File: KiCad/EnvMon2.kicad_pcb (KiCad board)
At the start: 2 copper layers, 57.5 x 37 mm, 35 parts, among them J1 USB-C, J2 DC, J3 TEMP, M1 OLED1.5-RGB, SW1 SW_Push, SW2 SW_Push, SW3 SW_Push, U1 LMR16006+FB, U2 SCD41, U3 FT231XQ, U4 ESP32-PICO-MINI-02, U5 QR

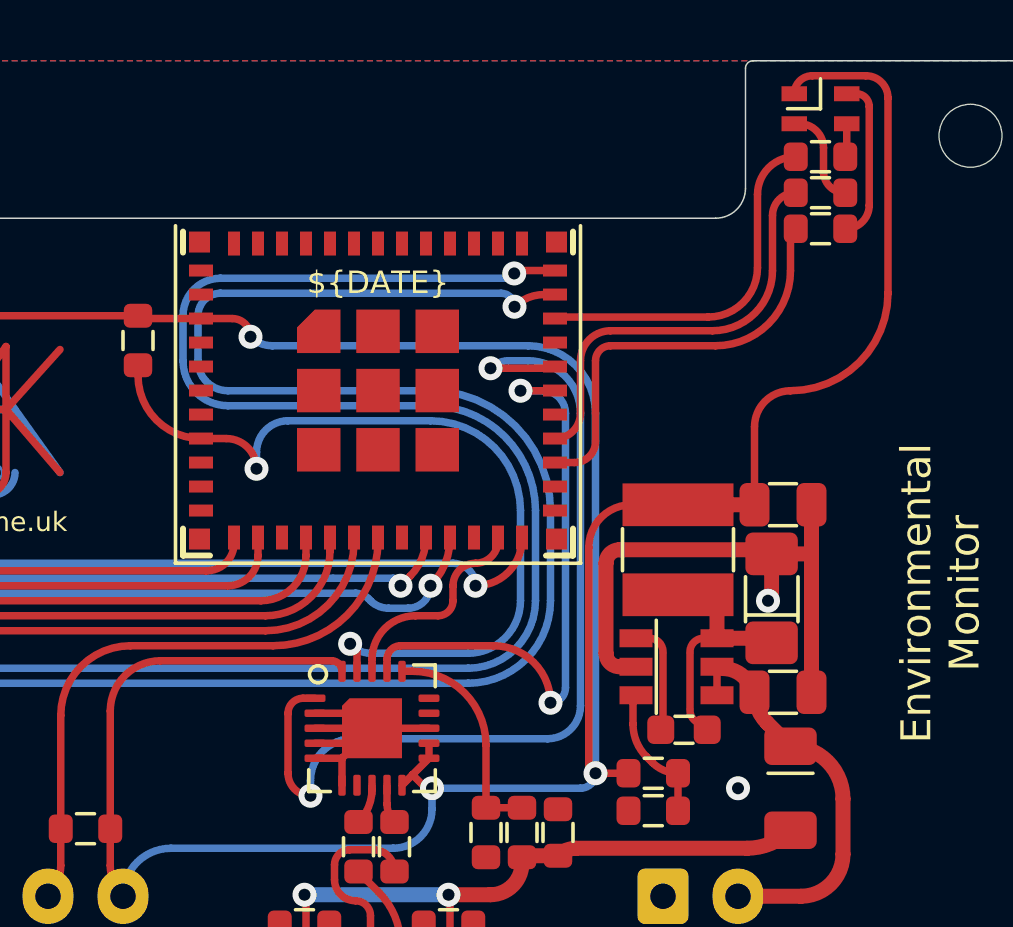
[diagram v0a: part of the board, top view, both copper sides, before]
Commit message: Updated regulator
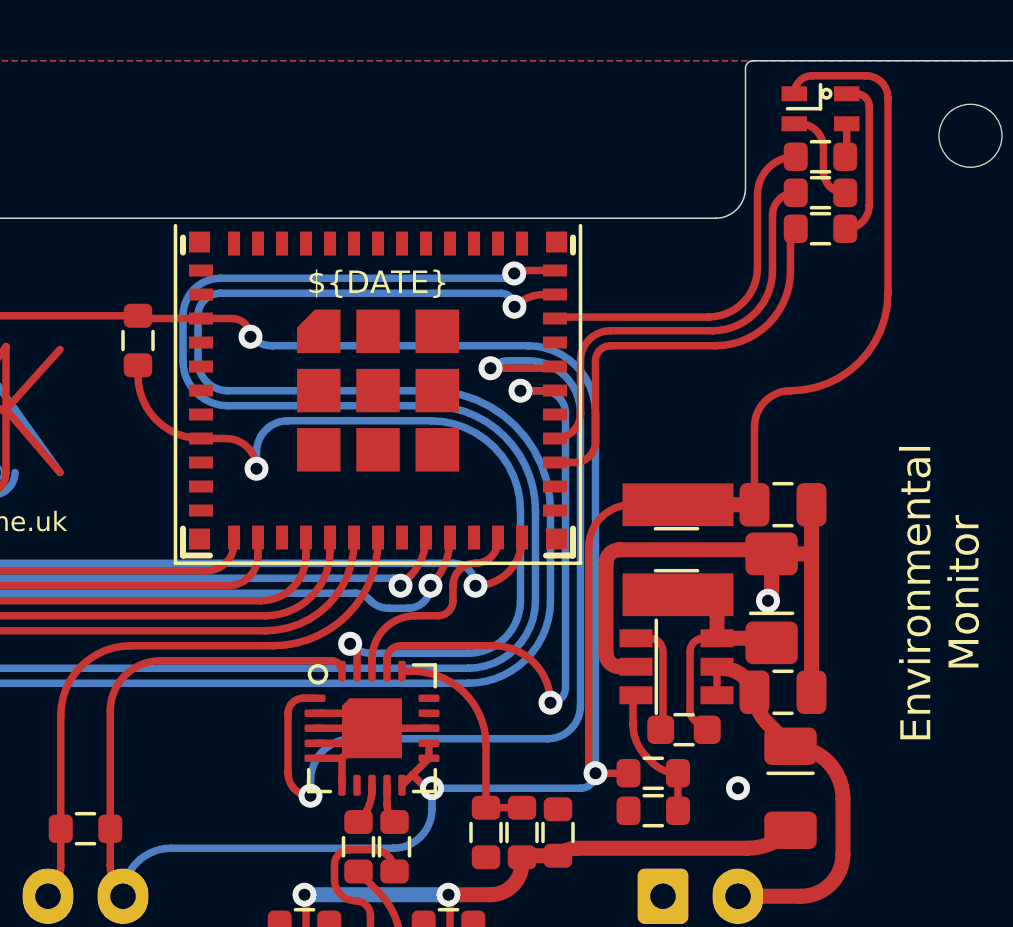
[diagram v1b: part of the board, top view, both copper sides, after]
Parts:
- C1: value 0.1uF -> 100nF; footprint RevK:Hidden -> RevK:C_0603_
- C2, C3: footprint RevK:Hidden -> RevK:C_0805_
- D1: footprint RevK:Hidden -> RevK:D_1206_
- L1: footprint RevK:Hidden -> RevK:L_4x4_

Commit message: Some PCB rework in progress
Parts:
- added J4: Shelly, RevK:Shelly, F.Cu at (141.7, 81.0)
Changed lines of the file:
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@@
     )
+  )
+  (footprint "RevK:Shelly" (layer "F.Cu")
+    (at 141.7 81 90)
+    (property "Sheetfile" "EnvMon2.kicad_sch")
+    (property "Sheetname" "")
+    (property "exclude_from_bom" "")
+    (attr through_hole exclude_from_bom)
+    (fp_text reference "J4" (at 0 -2.6 90 unlocked) (layer "F.SilkS") hide
+      (effects (font (size 1 1) (thickness 0.15)))
+    )
+    (fp_text value "Shelly" (at 0.2 3.7 90 unlocked) (layer "F.Fab") hide
+      (effects (font (size 1 1) (thickness 0.15)))
+    )
+    (fp_text user "⏚" (at 4.25 -0.8 135 unlocked) (layer "F.SilkS")
+      (effects (font (size 0.5 0.5) (thickness 0.08)))
+    )
+    (fp_text user "↑3" (at -3.37 -0.8 135 unlocked) (layer "F.SilkS")
+      (effects (font (size 0.5 0.5) (thickness 0.08)))
+    )
+    (fp_text user "0" (at 1.71 -0.8 135 unlocked) (layer "F.SilkS")
+      (effects (font (size 0.5 0.5) (thickness 0.08)))
+    )
+    (fp_text user "3V3" (at -0.83 -0.8 135 unlocked) (layer "F.SilkS")
+      (effects (font (size 0.5 0.5) (thickness 0.08)))
+    )
+    (fp_text user "↓1" (at -5.91 -0.8 135 unlocked) (layer "F.SilkS")
+      (effects (font (size 0.5 0.5) (thickness 0.08)))
+    )
+    (fp_text user "${REFERENCE}" (at 0 -2.6 90) (layer "F.Fab")
+      (effects (font (size 1 1) (thickness 0.15)))
+    )
+    (pad "1" thru_hole roundrect (at 5.08 0 90) (size 1.7 1.7) (drill 1) (layers *.Cu *.Mask) (roundrect_rratio 0)
+      (chamfer_ratio 0.3) (chamfer top_left)
+      (net 38 "O") (pinfunction "GND") (pintype "passive"))
+    (pad "2" thru_hole oval (at 2.54 0) (size 1.7 1.7) (drill 1) (layers *.Cu *.Mask)
+      (net 42 "I") (pinfunction "0") (pintype "passive"))
+    (pad "3" thru_hole oval (at 0 0) (size 1.7 1.7) (drill 1) (layers *.Cu *.Mask)
+      (net 12 "+3V3") (pinfunction "3V3") (pintype "passive"))
+    (pad "4" thru_hole oval (at -2.54 0) (size 1.7 1.7) (drill 1) (layers *.Cu *.Mask)
+      (net 47 "BOOT") (pinfunction "Rx") (pintype "passive"))
+    (pad "5" thru_hole oval (at -5.08 0) (size 1.7 1.7) (drill 1) (layers *.Cu *.Mask)
+      (net 11 "GND") (pinfunction "Tx") (pintype "passive"))
   )
   (footprint "RevK:C_0603_" (layer "F.Cu")

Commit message: Revised PCB for light sensor
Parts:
- added U6: VEML3235SL, RevK:VEML3235SL, F.Cu at (106.2, 63.8)
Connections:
- net CO2-SCL renamed SCL
- net CO2-SDA renamed SDA
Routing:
- net SDA: track 86.1 -> 114.7 mm, vias 2 -> 3
- net +3V3: track 151.9 -> 177.8 mm
- net BOOT: track 7.04 -> 31.7 mm, vias 0 -> 1
- net I: track 20.1 -> 37.1 mm, vias 2 -> 3
- net O: track 31.1 -> 47.9 mm, vias 2 -> 3
- net SCL: track 89.4 -> 104.5 mm, vias 2 -> 3
- net GND: track 12.1 -> 20.6 mm, vias 10 -> 12
- net R: track 14.0 -> 13.5 mm
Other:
- outline, holes or cut-outs redrawn

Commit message: Right angle
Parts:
- U6: value VEML3235SL -> VEML3235SL-RA; footprint RevK:VEML3235SL -> RevK:VEML3235SL-RA
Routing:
- net +3V3: track 177.8 -> 179.8 mm
- net SCL: track 104.5 -> 106.3 mm
- net SDA: track 114.7 -> 115.3 mm

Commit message: Library update
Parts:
- moved U6 1.40 mm to (107.6, 63.8)
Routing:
- net +3V3: track 179.8 -> 178.2 mm
- net SCL: track 106.3 -> 105.5 mm
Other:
- outline, holes or cut-outs redrawn

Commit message: Minor tweaks
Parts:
- J1: footprint RevK:USC16-TR-Round -> RevK:USC16-TR
- moved Logo1 0.95 mm to (109.6, 74.6)
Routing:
- net VBUS: track 22.2 -> 26.7 mm

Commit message: Library update
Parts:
- turned J4 to -90 degrees
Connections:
- J4 pad 1: O -> GND
- J4 pad 2: I -> BOOT
- J4 pad 4: BOOT -> I
- J4 pad 5: GND -> O
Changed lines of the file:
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@@
     )
   )
-  (property "DATE" "2022-11-28")
+  (property "DATE" "2022-12-14")
   (net 0 "")
   (net 1 "VBUS")
@@
   )
   (footprint "RevK:Shelly" (layer "F.Cu")
-    (at 141.7 81 90)
+    (at 141.7 81 -90)
     (property "Sheetfile" "EnvMon2.kicad_sch")
     (property "Sheetname" "")
     (property "exclude_from_bom" "")
     (attr through_hole exclude_from_bom)
-    (fp_text reference "J4" (at 0 -2.6 90 unlocked) (layer "F.SilkS") hide
-      (effects (font (size 1 1) (thickness 0.15)))
-    )
-    (fp_text value "Shelly" (at 0.2 3.7 90 unlocked) (layer "F.Fab") hide
-      (effects (font (size 1 1) (thickness 0.15)))
-    )
-    (fp_text user "3V3" (at -0.83 -0.8 135 unlocked) (layer "F.SilkS")
-      (effects (font (size 0.5 0.5) (thickness 0.08)))
-    )
-    (fp_text user "⏚" (at 4.25 -0.8 135 unlocked) (layer "F.SilkS")
-      (effects (font (size 0.5 0.5) (thickness 0.08)))
-    )
-    (fp_text user "↓1" (at -5.91 -0.8 135 unlocked) (layer "F.SilkS")
-      (effects (font (size 0.5 0.5) (thickness 0.08)))
-    )
-    (fp_text user "0" (at 1.71 -0.8 135 unlocked) (layer "F.SilkS")
-      (effects (font (size 0.5 0.5) (thickness 0.08)))
-    )
-    (fp_text user "↑3" (at -3.37 -0.8 135 unlocked) (layer "F.SilkS")
+    (fp_text reference "J4" (at 0 -2.6 -90 unlocked) (layer "F.SilkS") hide
+      (effects (font (size 1 1) (thickness 0.15)))
+    )
+    (fp_text value "Shelly" (at 0.2 3.7 -90 unlocked) (layer "F.Fab") hide
+      (effects (font (size 1 1) (thickness 0.15)))
+    )
+    (fp_text user "3V3" (at -0.83 -0.8 -45 unlocked) (layer "F.SilkS")
+      (effects (font (size 0.5 0.5) (thickness 0.08)))
+    )
+    (fp_text user "⏚" (at 4.25 -0.8 -45 unlocked) (layer "F.SilkS")
+      (effects (font (size 0.5 0.5) (thickness 0.08)))
+    )
+    (fp_text user "↓1" (at -5.91 -0.8 -45 unlocked) (layer "F.SilkS")
+      (effects (font (size 0.5 0.5) (thickness 0.08)))
+    )
+    (fp_text user "0" (at 1.71 -0.8 -45 unlocked) (layer "F.SilkS")
+      (effects (font (size 0.5 0.5) (thickness 0.08)))
+    )
+    (fp_text user "↑3" (at -3.37 -0.8 -45 unlocked) (layer "F.SilkS")
       (effects (font (size 0.5 0.5) (thickness 0.08)))
     )
@@
       (effects (font (size 1 1) (thickness 0.15)))
     )
-    (pad "1" thru_hole roundrect (at 5.08 0 90) (size 1.7 1.7) (drill 1) (layers *.Cu *.Mask) (roundrect_rratio 0)
+    (pad "1" thru_hole roundrect (at 5.08 0 270) (size 1.7 1.7) (drill 1) (layers *.Cu *.Mask) (roundrect_rratio 0)
       (chamfer_ratio 0.3) (chamfer top_left)
-      (net 38 "O") (pinfunction "GND") (pintype "passive"))
-    (pad "2" thru_hole oval (at 2.54 0) (size 1.7 1.7) (drill 1) (layers *.Cu *.Mask)
-      (net 42 "I") (pinfunction "0") (pintype "passive"))
-    (pad "3" thru_hole oval (at 0 0) (size 1.7 1.7) (drill 1) (layers *.Cu *.Mask)
+      (net 11 "GND") (pinfunction "GND") (pintype "passive"))
+    (pad "2" thru_hole oval (at 2.54 0 180) (size 1.7 1.7) (drill 1) (layers *.Cu *.Mask)
+      (net 47 "BOOT") (pinfunction "0") (pintype "passive"))
+    (pad "3" thru_hole oval (at 0 0 180) (size 1.7 1.7) (drill 1) (layers *.Cu *.Mask)
       (net 12 "+3V3") (pinfunction "3V3") (pintype "passive"))
-    (pad "4" thru_hole oval (at -2.54 0) (size 1.7 1.7) (drill 1) (layers *.Cu *.Mask)
-      (net 47 "BOOT") (pinfunction "Rx") (pintype "passive"))
-    (pad "5" thru_hole oval (at -5.08 0) (size 1.7 1.7) (drill 1) (layers *.Cu *.Mask)
-      (net 11 "GND") (pinfunction "Tx") (pintype "passive"))
+    (pad "4" thru_hole oval (at -2.54 0 180) (size 1.7 1.7) (drill 1) (layers *.Cu *.Mask)
+      (net 42 "I") (pinfunction "Rx") (pintype "passive"))
+    (pad "5" thru_hole oval (at -5.08 0 180) (size 1.7 1.7) (drill 1) (layers *.Cu *.Mask)
+      (net 38 "O") (pinfunction "Tx") (pintype "passive"))
   )
   (footprint "RevK:C_0603_" (layer "F.Cu")

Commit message: PCBs
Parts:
- added ?: , RevK:PasteEnvMon2, F.Cu at (107.5, 112.2)
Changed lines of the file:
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@@
     )
+  )
+  (footprint "RevK:PasteEnvMon2" (layer "F.Cu")
+    (at 107.45 112.15)
+    (attr exclude_from_pos_files exclude_from_bom)
+    (fp_text reference "" (at 0 0) (layer "F.SilkS")
+      (effects (font (size 1.27 1.27) (thickness 0.15)))
+    )
+    (fp_text value "" (at 0 0) (layer "F.SilkS")
+      (effects (font (size 1.27 1.27) (thickness 0.15)))
+    )
+    (pad "" smd circle locked (at 20.145 0.255) (size 0.45 0.45) (layers "F.Paste"))
+    (pad "" smd circle locked (at 11.475 2.295) (size 0.45 0.45) (layers "F.Paste"))
+    (pad "" smd circle locked (at 19.635 0.255) (size 0.45 0.45) (layers "F.Paste"))
+    (pad "" smd circle locked (at 18.615 2.805) (size 0.45 0.45) (layers "F.Paste"))
+    (pad "" smd circle locked (at 12.495 1.785) (size 0.45 0.45) (layers "F.Paste"))
+    (pad "" smd circle locked (at 5.355 2.805) (size 0.45 0.45) (layers "F.Paste"))
+    (pad "" smd circle locked (at 20.655 3.315) (size 0.45 0.45) (layers "F.Paste"))
+    (pad "" smd circle locked (at 0.255 0.765) (size 0.45 0.45) (layers "F.Paste"))
+    (pad "" smd circle locked (at 4.335 1.275) (size 0.45 0.45) (layers "F.Paste"))
+    (pad "" smd circle locked (at 1.275 0.255) (size 0.45 0.45) (layers "F.Paste"))
+    (pad "" smd circle locked (at 0.255 3.315) (size 0.45 0.45) (layers "F.Paste"))
+    (pad "" smd circle locked (at 18.615 0.765) (size 0.45 0.45) (layers "F.Paste"))
+    (pad "" smd circle locked (at 19.635 3.315) (size 0.45 0.45) (layers "F.Paste"))
+    (pad "" smd circle locked (at 13.515 1.275) (size 0.45 0.45) (layers "F.Paste"))
+    (pad "" smd circle locked (at 6.885 2.805) (size 0.45 0.45) (layers "F.Paste"))
+    (pad "" smd circle locked (at 20.145 1.785) (size 0.45 0.45) (layers "F.Paste"))
+    (pad "" smd circle locked (at 18.615 3.315) (size 0.45 0.45) (layers "F.Paste"))
+    (pad "" smd circle locked (at 12.495 2.805) (size 0.45 0.45) (layers "F.Paste"))
+    (pad "" smd circle locked (at 10.455 1.785) (size 0.45 0.45) (layers "F.Paste"))
+    (pad "" smd circle locked (at 1.785 1.785) (size 0.45 0.45) (layers "F.Paste"))
+    (pad "" smd circle locked (at 2.295 3.315) (size 0.45 0.45) (layers "F.Paste"))
+    (pad "" smd circle locked (at 19.125 2.295) (size 0.45 0.45) (layers "F.Paste"))
+    (pad "" smd circle locked (at 11.475 1.275) (size 0.45 0.45) (layers "F.Paste"))
+    (pad "" smd circle locked (at 19.125 0.255) (size 0.45 0.45) (layers "F.Paste"))
+    (pad "" smd circle locked (at 15.555 2.295) (size 0.45 0.45) (layers "F.Paste"))
+    (pad "" smd circle locked (at 19.125 3.315) (size 0.45 0.45) (layers "F.Paste"))
+    (pad "" smd circle locked (at 9.945 0.765) (size 0.45 0.45) (layers "F.Paste"))
+    (pad "" smd circle locked (at 9.435 1.275) (size 0.45 0.45) (layers "F.Paste"))
+    (pad "" smd circle locked (at 9.435 0.255) (size 0.45 0.45) (layers "F.Paste"))
+    (pad "" smd circle locked (at 17.085 1.275) (size 0.45 0.45) (layers "F.Paste"))
+    (pad "" smd circle locked (at 11.475 1.785) (size 0.45 0.45) (layers "F.Paste"))
+    (pad "" smd circle locked (at 9.435 2.805) (size 0.45 0.45) (layers "F.Paste"))
+    (pad "" smd circle locked (at 12.495 2.295) (size 0.45 0.45) (layers "F.Paste"))
+    (pad "" smd circle locked (at 10.965 0.765) (size 0.45 0.45) (layers "F.Paste"))
+    (pad "" smd circle locked (at 9.435 0.765) (size 0.45 0.45) (layers "F.Paste"))
+    (pad "" smd circle locked (at 3.315 2.805) (size 0.45 0.45) (layers "F.Paste"))
+    (pad "" smd circle locked (at 5.355 3.315) (size 0.45 0.45) (layers "F.Paste"))
+    (pad "" smd circle locked (at 0.765 3.315) (size 0.45 0.45) (layers "F.Paste"))
+    (pad "" smd circle locked (at 0.765 0.255) (size 0.45 0.45) (layers "F.Paste"))
+    (pad "" smd circle locked (at 13.515 3.315) (size 0.45 0.45) (layers "F.Paste"))
+    (pad "" smd circle locked (at 5.355 1.785) (size 0.45 0.45) (layers "F.Paste"))
+    (pad "" smd circle locked (at 7.905 2.805) (size 0.45 0.45) (layers "F.Paste"))
+    (pad "" smd circle locked (at 3.315 3.315) (size 0.45 0.45) (layers "F.Paste"))
+    (pad "" smd circle locked (at 1.275 3.315) (size 0.45 0.45) (layers "F.Paste"))
+    (pad "" smd circle locked (at 14.535 2.295) (size 0.45 0.45) (layers "F.Paste"))
+    (pad "" smd circle locked (at 3.315 1.275) (size 0.45 0.45) (layers "F.Paste"))
+    (pad "" smd circle locked (at 0.255 1.785) (size 0.45 0.45) (layers "F.Paste"))
+    (pad "" smd circle locked (at 1.275 1.785) (size 0.45 0.45) (layers "F.Paste"))
+    (pad "" smd circle locked (at 17.595 2.805) (size 0.45 0.45) (layers "F.Paste"))
+    (pad "" smd circle locked (at 3.825 1.275) (size 0.45 0.45) (layers "F.Paste"))
+    (pad "" smd circle locked (at 1.785 0.255) (size 0.45 0.45) (layers "F.Paste"))
+    (pad "" smd circle locked (at 0.255 0.255) (size 0.45 0.45) (layers "F.Paste"))
+    (pad "" smd circle locked (at 6.885 2.295) (size 0.45 0.45) (layers "F.Paste"))
+    (pad "" smd circle locked (at 15.555 3.315) (size 0.45 0.45) (layers "F.Paste"))
+    (pad "" smd circle locked (at 15.555 1.275) (size 0.45 0.45) (layers "F.Paste"))
+    (pad "" smd circle locked (at 19.635 1.785) (size 0.45 0.45) (layers "F.Paste"))
+    (pad "" smd circle locked (at 11.475 0.255) (size 0.45 0.45) (layers "F.Paste"))
+    (pad "" smd circle locked (at 16.575 1.275) (size 0.45 0.45) (layers "F.Paste"))
+    (pad "" smd circle locked (at 15.555 2.805) (size 0.45 0.45) (layers "F.Paste"))
+    (pad "" smd circle locked (at 13.005 3.315) (size 0.45 0.45) (layers "F.Paste"))
+    (pad "" smd circle locked (at 0.255 1.275) (size 0.45 0.45) (layers "F.Paste"))
+    (pad "" smd circle locked (at 11.475 2.805) (size 0.45 0.45) (layers "F.Paste"))
+    (pad "" smd circle locked (at 14.025 1.275) (size 0.45 0.45) (layers "F.Paste"))
+    (pad "" smd circle locked (at 4.845 1.275) (size 0.45 0.45) (layers "F.Paste"))
+    (pad "" smd circle locked (at 17.595 3.315) (size 0.45 0.45) (layers "F.Paste"))
+    (pad "" smd circle locked (at 0.255 2.805) (size 0.45 0.45) (layers "F.Paste"))
+    (pad "" smd circle locked (at 0.765 1.785) (size 0.45 0.45) (layers "F.Paste"))
+    (pad "" smd circle locked (at 3.315 1.785) (size 0.45 0.45) (layers "F.Paste"))
+    (pad "" smd circle locked (at 9.435 3.315) (size 0.45 0.45) (layers "F.Paste"))
+    (pad "" smd circle locked (at 13.005 1.275) (size 0.45 0.45) (layers "F.Paste"))
+    (pad "" smd circle locked (at 20.655 0.765) (size 0.45 0.45) (layers "F.Paste"))
+    (pad "" smd circle locked (at 14.535 2.805) (size 0.45 0.45) (layers "F.Paste"))
+    (pad "" smd circle locked (at 17.595 2.295) (size 0.45 0.45) (layers "F.Paste"))
+    (pad "" smd circle locked (at 9.435 1.785) (size 0.45 0.45) (layers "F.Paste"))
+    (pad "" smd circle locked (at 11.475 0.765) (size 0.45 0.45) (layers "F.Paste"))
+    (pad "" smd circle locked (at 16.065 1.275) (size 0.45 0.45) (layers "F.Paste"))
+    (pad "" smd circle locked (at 0.255 2.295) (size 0.45 0.45) (layers "F.Paste"))
+    (pad "" smd circle locked (at 5.355 2.295) (size 0.45 0.45) (layers "F.Paste"))
+    (pad "" smd circle locked (at 20.145 3.315) (size 0.45 0.45) (layers "F.Paste"))
+    (pad "" smd circle locked (at 8.415 1.275) (size 0.45 0.45) (layers "F.Paste"))
+    (pad "" smd circle locked (at 2.295 0.255) (size 0.45 0.45) (layers "F.Paste"))
+    (pad "" smd circle locked (at 7.905 2.295) (size 0.45 0.45) (layers "F.Paste"))
+    (pad "" smd circle locked (at 14.535 1.785) (size 0.45 0.45) (layers "F.Paste"))
+    (pad "" smd circle locked (at 7.395 3.315) (size 0.45 0.45) (layers "F.Paste"))
+    (pad "" smd circle locked (at 10.455 1.275) (size 0.45 0.45) (layers "F.Paste"))
+    (pad "" smd circle locked (at 8.415 1.785) (size 0.45 0.45) (layers "F.Paste"))
+    (pad "" smd circle locked (at 1.785 3.315) (size 0.45 0.45) (layers "F.Paste"))
+    (pad "" smd circle locked (at 17.595 1.785) (size 0.45 0.45) (layers "F.Paste"))
+    (pad "" smd circle locked (at 9.435 2.295) (size 0.45 0.45) (layers "F.Paste"))
+    (pad "" smd circle locked (at 15.555 1.785) (size 0.45 0.45) (layers "F.Paste"))
+    (pad "" smd circle locked (at 14.025 3.315) (size 0.45 0.45) (layers "F.Paste"))
+    (pad "" smd circle locked (at 3.315 2.295) (size 0.45 0.45) (layers "F.Paste"))
+    (pad "" smd circle locked (at 6.375 1.785) (size 0.45 0.45) (layers "F.Paste"))
+    (pad "" smd circle locked (at 6.375 1.275) (size 0.45 0.45) (layers "F.Paste"))
+    (pad "" smd circle locked (at 11.475 3.315) (size 0.45 0.45) (layers "F.Paste"))
+    (pad "" smd circle locked (at 20.655 1.275) (size 0.45 0.45) (layers "F.Paste"))
   )
   (footprint "Button_Switch_THT:SW_PUSH_6mm_H13mm" (layer "F.Cu")
